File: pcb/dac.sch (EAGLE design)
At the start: 23 parts, among them U1 PIC16F1773-I/SP, U2 MCP6002-I/P

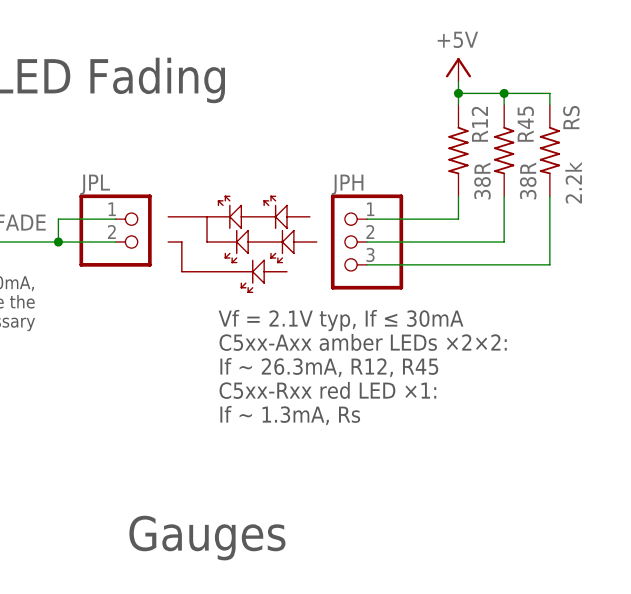
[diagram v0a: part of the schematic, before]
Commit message: Ended up using 1k for power indicator; journal entry
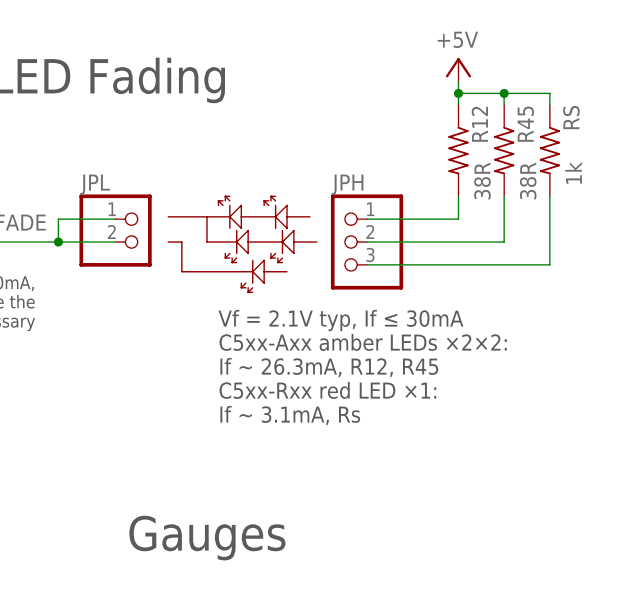
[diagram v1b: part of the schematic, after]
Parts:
- RS: value 2.2k -> 1k
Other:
- note added: "Vf = 2.1V typ, If ≤ 30mA C5xx-Axx amber LEDs ×2×2: If ~ 26.3mA, R12, R45 C5xx-Rxx red LED ×1: If ~ 3.1mA, Rs"
- note removed: "Vf = 2.1V typ, If ≤ 30mA C5xx-Axx amber LEDs ×2×2: If ~ 26.3mA, R12, R45 C5xx-Rxx red LED ×1: If ~ 1.3mA, Rs"
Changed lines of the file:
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@@
 <part name="JG5H" library="pinhead" library_urn="urn:adsk.eagle:library:325" deviceset="PINHD-1X1" device="" package3d_urn="urn:adsk.eagle:package:22485/2"/>
 <part name="JG5L" library="pinhead" library_urn="urn:adsk.eagle:library:325" deviceset="PINHD-1X1" device="" package3d_urn="urn:adsk.eagle:package:22485/2"/>
-<part name="RS" library="rcl" library_urn="urn:adsk.eagle:library:334" deviceset="R-US_" device="0207/2V" package3d_urn="urn:adsk.eagle:package:23490/1" value="2.2k"/>
+<part name="RS" library="rcl" library_urn="urn:adsk.eagle:library:334" deviceset="R-US_" device="0207/2V" package3d_urn="urn:adsk.eagle:package:23490/1" value="1k"/>
 <part name="RP" library="rcl" library_urn="urn:adsk.eagle:library:334" deviceset="R-US_" device="0207/5V" package3d_urn="urn:adsk.eagle:package:23502/1" value="1k"/>
 <part name="+3V1" library="supply1" library_urn="urn:adsk.eagle:library:371" deviceset="+3V3" device=""/>
@@
 If ~ 26.3mA, R12, R45
 C5xx-Rxx red LED ×1:
-If ~ 1.3mA, Rs</text>
+If ~ 3.1mA, Rs</text>
 <text x="106.68" y="167.64" size="1.016" layer="97">For layout
 ease, unused</text>

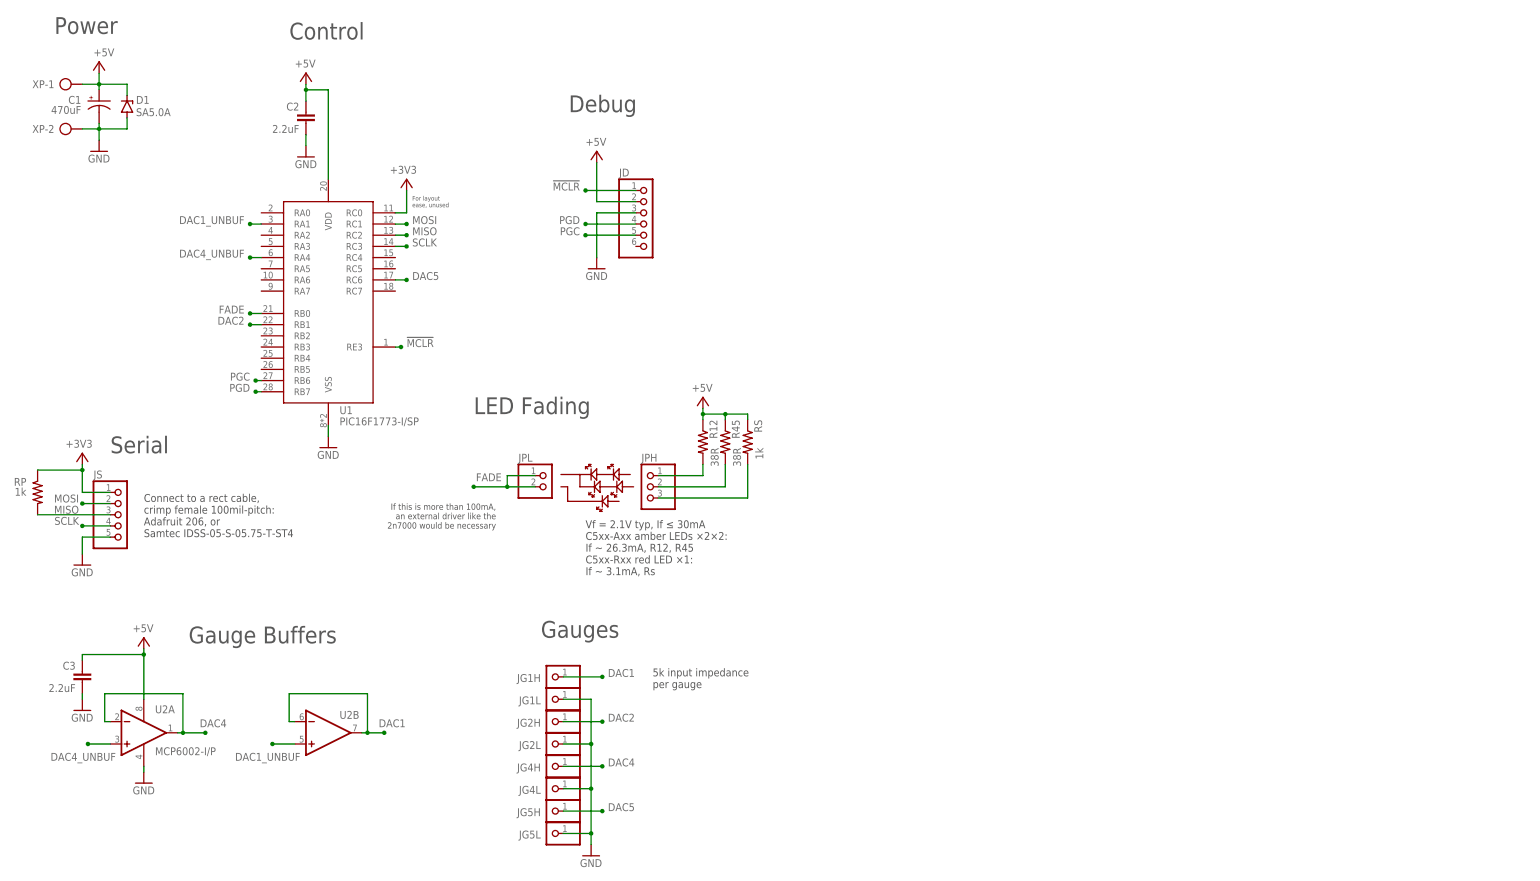
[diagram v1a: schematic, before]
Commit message: New layout with larger board and level shifter
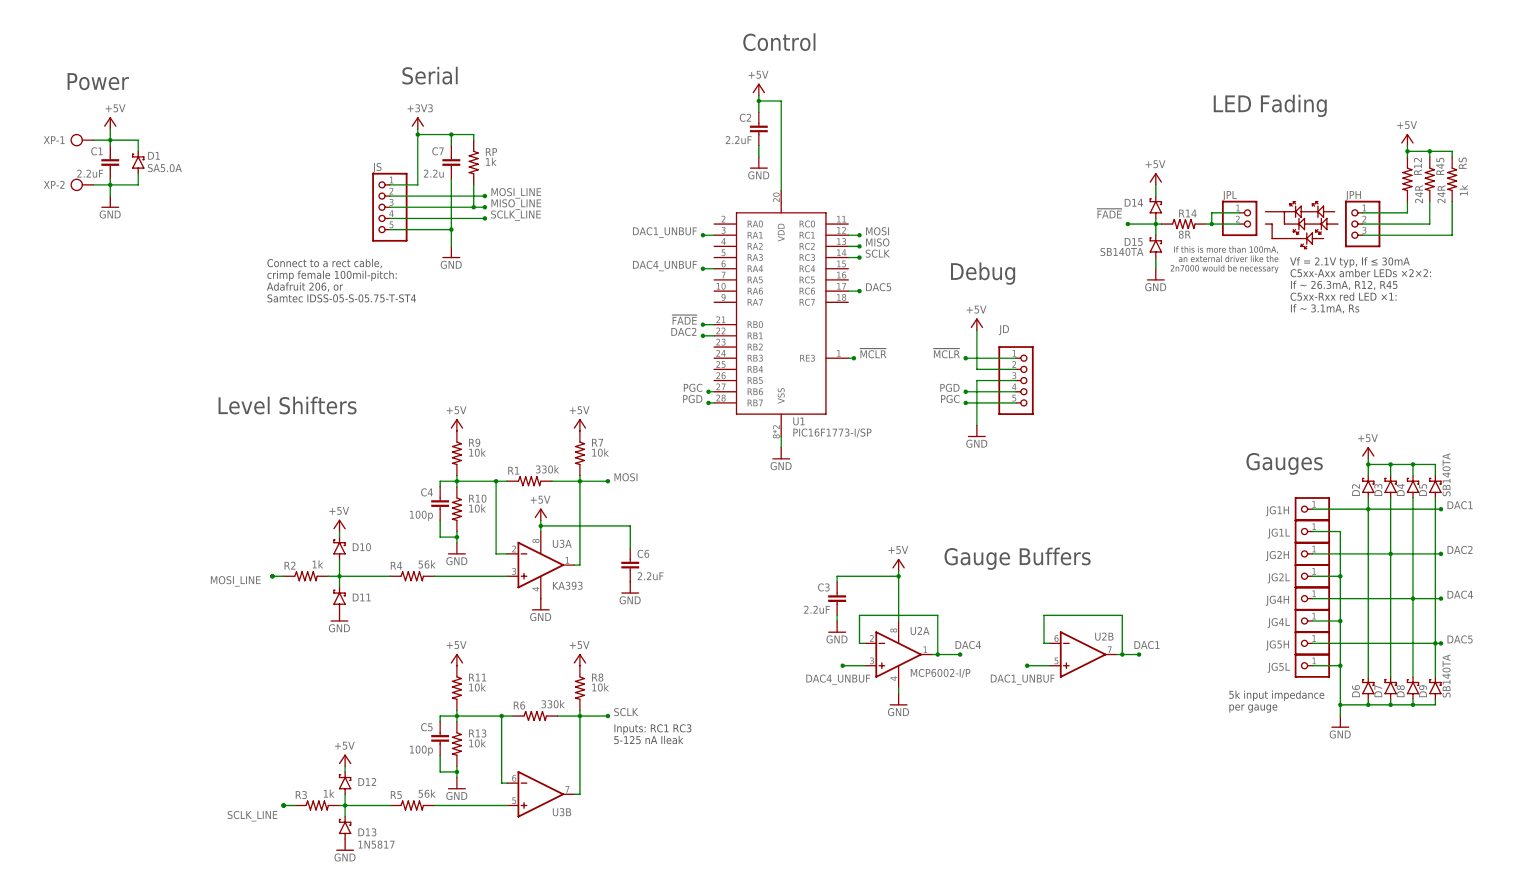
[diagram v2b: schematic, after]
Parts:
- added C4, C5: 100p, rcl:C-EU050-024X044
- added C6: 2.2uF, rcl:C-EU050-024X044
- added C7: 2.2u, rcl:C-EU050-024X044
- added D10: 1N5817-H76, diode-vertical:1N5817-H76
- added D11: 1N5817-V, diode-vertical:1N5817-V
- added D12: 1N5817-T, diode:1N5817-T
- added D13: 1N5817, diode-vertical:1N5817-H10
- added D14, D15: SB140TA, diode-vertical:SB140-V
- added D2, D3, D4, D5, D6: SB140TA, diode-vertical:SB140
- added D7, D8, D9: SB140TA, diode:1N5817-B
- added R1, R6: 330k, rcl:R-US_0207/2V
- added R10, R11, R13: 10k, rcl:R-US_0207/5V
- added R14: 8R, rcl:R-US_0207/15
- added R2: 1k, rcl:R-US_0204/7
- added R3: 1k, rcl:R-US_0207/10
- added R4: 56k, rcl:R-US_0207/10
- added R5: 56k, rcl:R-US_0207/15
- added R7, R8: 10k, rcl:R-US_0207/2V
- added R9: 10k, rcl:R-US_0207/7
- added U3: KA393, linear:LM393N
- C1: value 470uF -> 2.2uF; device rcl:CPOL-USE3.5-8 -> rcl:C-EU050-024X044
- D1: device diode:1N821 -> diode-vertical:SB120-V
- JD: device pinhd-pol:PINHD-1X6-PICKIT -> pinhead:PINHD-1X5
- R12, R45: value 38R -> 24R
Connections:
- removed net FADE: JPL.1, JPL.2, U1.RB0
- new net !FADE: D14.A, D15.C, R14.1, U1.RB0
- new net !FADE_PROT: JPL.1, JPL.2, R14.2
- new net MISO_LINE: JS.3, RP.2
- new net MOSI_LINE: JS.2, R2.1
- new net MOSI_N: C4.1, R1.1, R10.1, R9.2, U3A.-IN
- new net MOSI_P: R4.2, U3A.+IN
- new net MOSI_PROT: D10.A, D11.C, R2.2, R4.1
- new net SCLK_LINE: JS.4, R3.1
- new net SCLK_N: C5.1, R11.2, R13.1, R6.1, U3B.-IN
- new net SCLK_P: R5.2, U3B.+IN
- new net SCLK_PROT: D12.A, D13.C, R3.2, R5.1
- net +3V3: now also C7.1; no longer U1.RC0
- net +5V: now also C1.1, C6.1, D10.C, D12.C, D14.C, D2.C, D3.C, D4.C, D5.C, R11.1, R7.1, R8.1, R9.1, U3P.V+; no longer C1.+
- net DAC1: now also D2.A, D6.C
- net DAC2: now also D3.A, D7.C
- net DAC4: now also D4.A, D8.C
- net DAC5: now also D5.A, D9.C
- net GND: now also C1.2, C4.2, C5.2, C6.2, C7.2, D11.A, D13.A, D15.A, D6.A, D7.A, D8.A, D9.A, R10.2, R13.2, U3P.V-; no longer C1.-
- net MISO: no longer JS.3, RP.2
- net MOSI: now also R1.2, R7.2, U3A.OUT; no longer JS.2
- net SCLK: now also R6.2, R8.2, U3B.OUT; no longer JS.4
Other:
- note added: "Inputs: RC1 RC3 5-125 nA Ileak"
- note added: "Level Shifters"
- note removed: "For layout ease, unused"
- moved on the sheet: C2, C3, JG1H, JG1L, JG2H, JG2L, JG4H, JG4L, JG5H, JG5L, JPH, JPL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

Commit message: MISO protection network, lower capacitance values, split jumper for LEDs
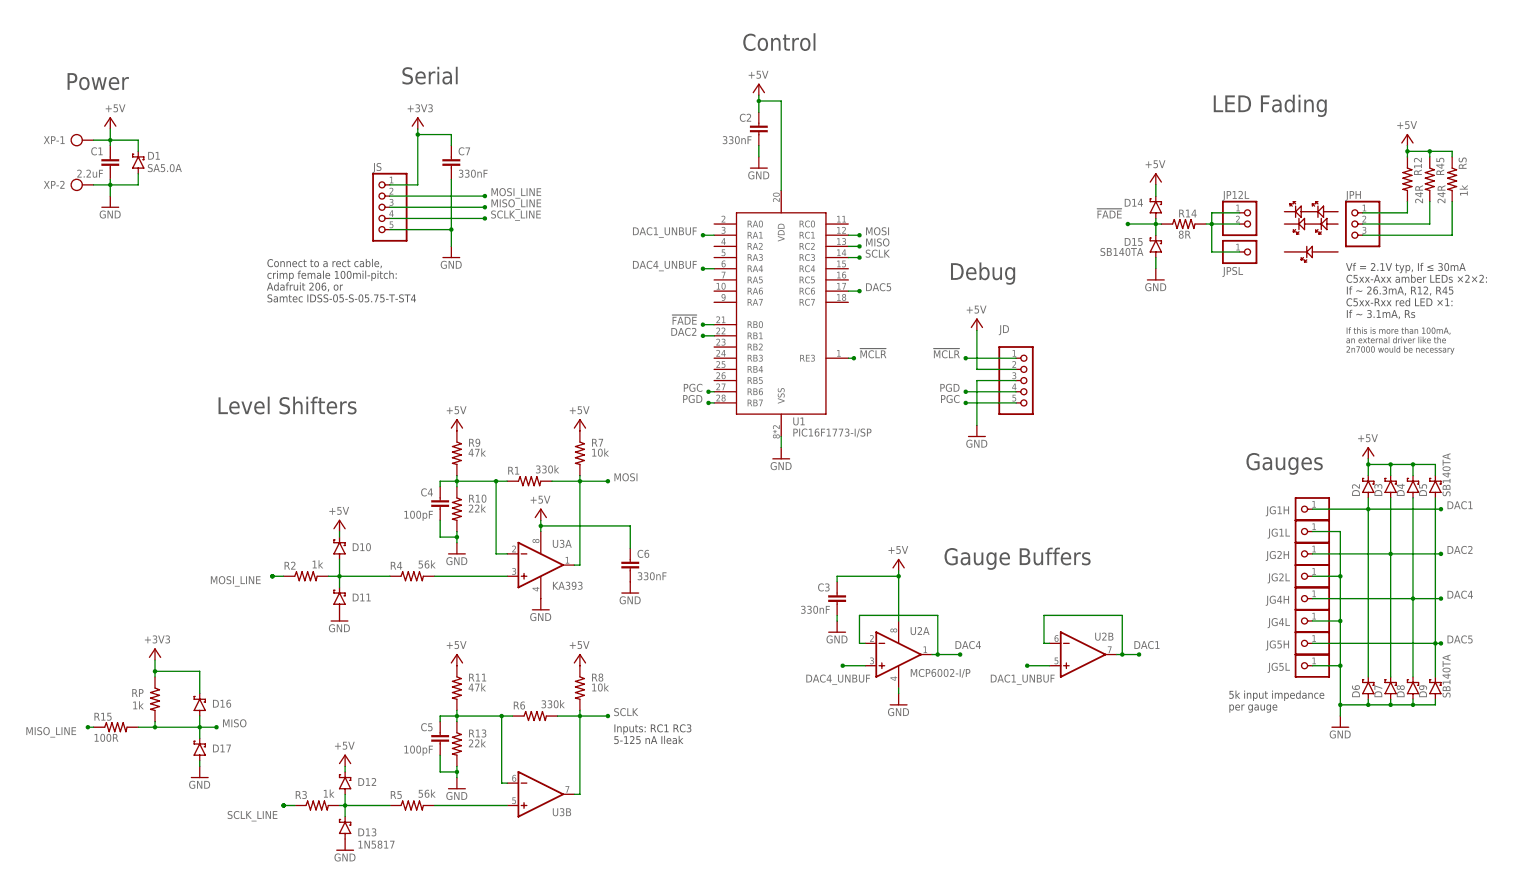
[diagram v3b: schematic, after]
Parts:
- added D16, D17: 1N5817-T, diode:1N5817-T
- added JPSL: (no value), pinhead:PINHD-1X1
- added R15: 100R, rcl:R-US_0207/10
- C2, C3, C6: value 2.2uF -> 330nF
- C4, C5: value 100p -> 100pF
- C7: value 2.2u -> 330nF
- R10, R13: value 10k -> 22k
- R11, R9: value 10k -> 47k
- R5: device rcl:R-US_0207/15 -> rcl:R-US_0207/12
- renumbered JPL to JP12L
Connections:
- net !FADE_PROT: now also JPSL.1
- net +3V3: now also D16.C
- net GND: now also D17.A
- net MISO: now also D16.A, D17.C, R15.2, RP.2
- net MISO_LINE: now also R15.1; no longer RP.2
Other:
- moved on the sheet: RP

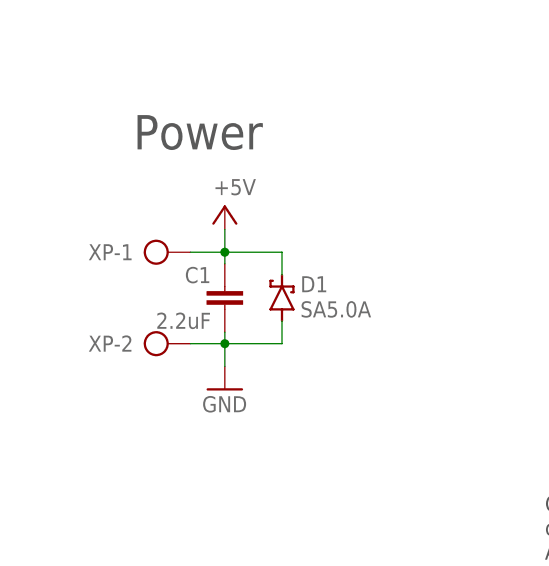
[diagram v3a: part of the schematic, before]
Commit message: Replace screw terminals with more header
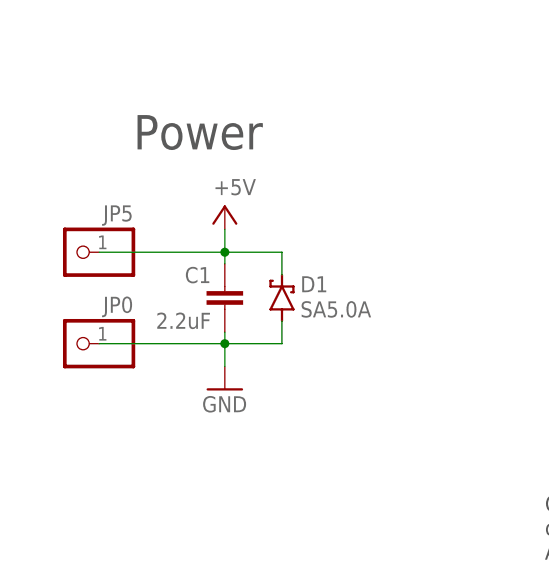
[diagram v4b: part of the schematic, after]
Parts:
- removed XP: (no value), con-wago-500:W237-102
- added JP0, JP5: (no value), pinhead:PINHD-1X1
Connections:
- net +5V: now also JP5.1; no longer XP-1.KL
- net GND: now also JP0.1; no longer XP-2.KL
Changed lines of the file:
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@@
 </classes>
 <parts>
-<part name="XP" library="con-wago-500" library_urn="urn:adsk.eagle:library:195" deviceset="W237-102" device="" package3d_urn="urn:adsk.eagle:package:10688/1"/>
 <part name="P+1" library="supply1" library_urn="urn:adsk.eagle:library:371" deviceset="+5V" device=""/>
 <part name="GND1" library="supply1" library_urn="urn:adsk.eagle:library:371" deviceset="GND" device=""/>
@@
 <part name="GND16" library="supply1" library_urn="urn:adsk.eagle:library:371" deviceset="GND" device=""/>
 <part name="JPSL" library="pinhead" library_urn="urn:adsk.eagle:library:325" deviceset="PINHD-1X1" device="" package3d_urn="urn:adsk.eagle:package:22485/2"/>
+<part name="JP5" library="pinhead" library_urn="urn:adsk.eagle:library:325" deviceset="PINHD-1X1" device="" package3d_urn="urn:adsk.eagle:package:22485/2"/>
+<part name="JP0" library="pinhead" library_urn="urn:adsk.eagle:library:325" deviceset="PINHD-1X1" device="" package3d_urn="urn:adsk.eagle:package:22485/2"/>
 </parts>
 <sheets>
@@
 </plain>
 <instances>
-<instance part="XP" gate="-1" x="29.21" y="182.88" smashed="yes">
-<attribute name="NAME" x="27.94" y="181.991" size="1.778" layer="95" rot="MR0"/>
-</instance>
-<instance part="XP" gate="-2" x="29.21" y="172.72" smashed="yes">
-<attribute name="VALUE" x="26.67" y="169.037" size="1.778" layer="96"/>
-<attribute name="NAME" x="27.94" y="171.831" size="1.778" layer="95" rot="MR0"/>
-</instance>
 <instance part="P+1" gate="1" x="38.1" y="187.96" smashed="yes">
 <attribute name="VALUE" x="36.83" y="189.23" size="1.778" layer="96"/>
@@
 <attribute name="NAME" x="290.83" y="152.273" size="1.778" layer="95"/>
 <attribute name="VALUE" x="290.83" y="152.4" size="1.778" layer="96"/>
+</instance>
+<instance part="JP5" gate="G$1" x="21.59" y="182.88" smashed="yes" rot="R180">
+<attribute name="NAME" x="27.94" y="188.087" size="1.778" layer="95" rot="R180"/>
+<attribute name="VALUE" x="27.94" y="187.96" size="1.778" layer="96" rot="R180"/>
+</instance>
+<instance part="JP0" gate="G$1" x="21.59" y="172.72" smashed="yes" rot="R180">
+<attribute name="NAME" x="27.94" y="177.927" size="1.778" layer="95" rot="R180"/>
+<attribute name="VALUE" x="27.94" y="177.8" size="1.778" layer="96" rot="R180"/>
 </instance>
 </instances>
@@
 <net name="+5V" class="1">
 <segment>
-<pinref part="XP" gate="-1" pin="KL"/>
 <pinref part="P+1" gate="1" pin="+5V"/>
-<wire x1="34.29" y1="182.88" x2="38.1" y2="182.88" width="0.1524" layer="91"/>
 <wire x1="38.1" y1="182.88" x2="38.1" y2="185.42" width="0.1524" layer="91"/>
 <wire x1="38.1" y1="181.61" x2="38.1" y2="182.88" width="0.1524" layer="91"/>
@@
 <wire x1="44.45" y1="182.88" x2="44.45" y2="180.34" width="0.1524" layer="91"/>
 <pinref part="C1" gate="G$1" pin="1"/>
+<wire x1="38.1" y1="182.88" x2="24.13" y2="182.88" width="0.1524" layer="91"/>
+<pinref part="JP5" gate="G$1" pin="1"/>
 </segment>
 <segment>
@@
 <segment>
 <pinref part="GND1" gate="1" pin="GND"/>
-<wire x1="38.1" y1="172.72" x2="34.29" y2="172.72" width="0.1524" layer="91"/>
-<pinref part="XP" gate="-2" pin="KL"/>
 <wire x1="38.1" y1="173.99" x2="38.1" y2="172.72" width="0.1524" layer="91"/>
 <wire x1="38.1" y1="172.72" x2="38.1" y2="170.18" width="0.1524" layer="91"/>
@@
 <wire x1="44.45" y1="172.72" x2="44.45" y2="175.26" width="0.1524" layer="91"/>
 <pinref part="C1" gate="G$1" pin="2"/>
-</segment>
-<segment>
+<wire x1="38.1" y1="172.72" x2="24.13" y2="172.72" width="0.1524" layer="91"/>
+<pinref part="JP0" gate="G$1" pin="1"/>
+</segment>
+<segment>

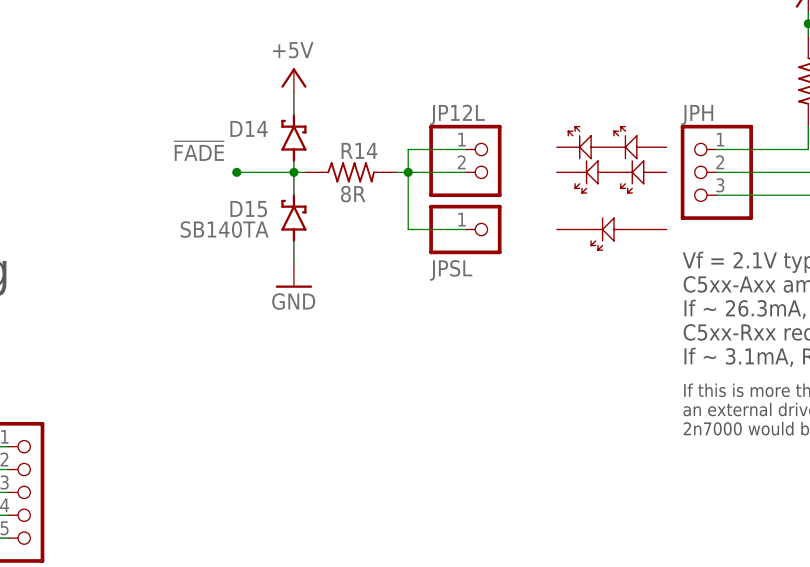
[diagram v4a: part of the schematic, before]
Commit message: Used different protection diodes for LEDs
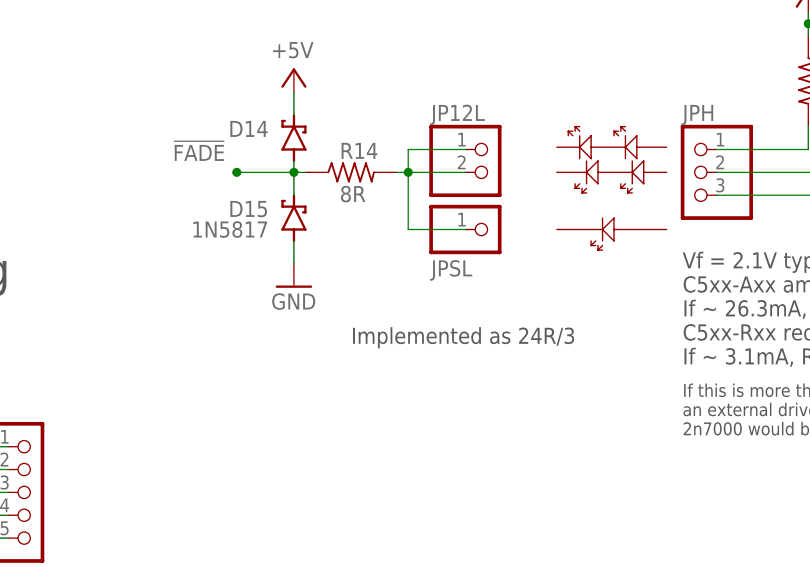
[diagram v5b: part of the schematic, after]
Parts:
- D14, D15: value SB140TA -> 1N5817
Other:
- note added: "Implemented as 24R/3"
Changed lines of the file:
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@@
 <part name="C7" library="rcl" library_urn="urn:adsk.eagle:library:334" deviceset="C-EU" device="050-024X044" package3d_urn="urn:adsk.eagle:package:23643/1" value="330nF"/>
 <part name="P+14" library="supply1" library_urn="urn:adsk.eagle:library:371" deviceset="+5V" device=""/>
-<part name="D14" library="diode-vertical" deviceset="SB" device="-V" technology="140" value="SB140TA"/>
-<part name="D15" library="diode-vertical" deviceset="SB" device="-V" technology="140" value="SB140TA"/>
+<part name="D14" library="diode-vertical" deviceset="SB" device="-V" technology="140" value="1N5817"/>
+<part name="D15" library="diode-vertical" deviceset="SB" device="-V" technology="140" value="1N5817"/>
 <part name="GND15" library="supply1" library_urn="urn:adsk.eagle:library:371" deviceset="GND" device=""/>
 <part name="R14" library="rcl" library_urn="urn:adsk.eagle:library:334" deviceset="R-US_" device="0207/15" package3d_urn="urn:adsk.eagle:package:23492/1" value="8R"/>
@@
 <text x="62.23" y="120.65" size="3.81" layer="97">Level Shifters</text>
 <frame x1="0" y1="0" x2="372.11" y2="220.98" columns="9" rows="6" layer="97"/>
+<text x="281.94" y="144.78" size="1.778" layer="97">Implemented as 24R/3</text>
 </plain>
 <instances>
